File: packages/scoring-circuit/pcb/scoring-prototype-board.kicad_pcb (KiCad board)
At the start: 2 copper layers, 160 x 100 mm, 46 parts

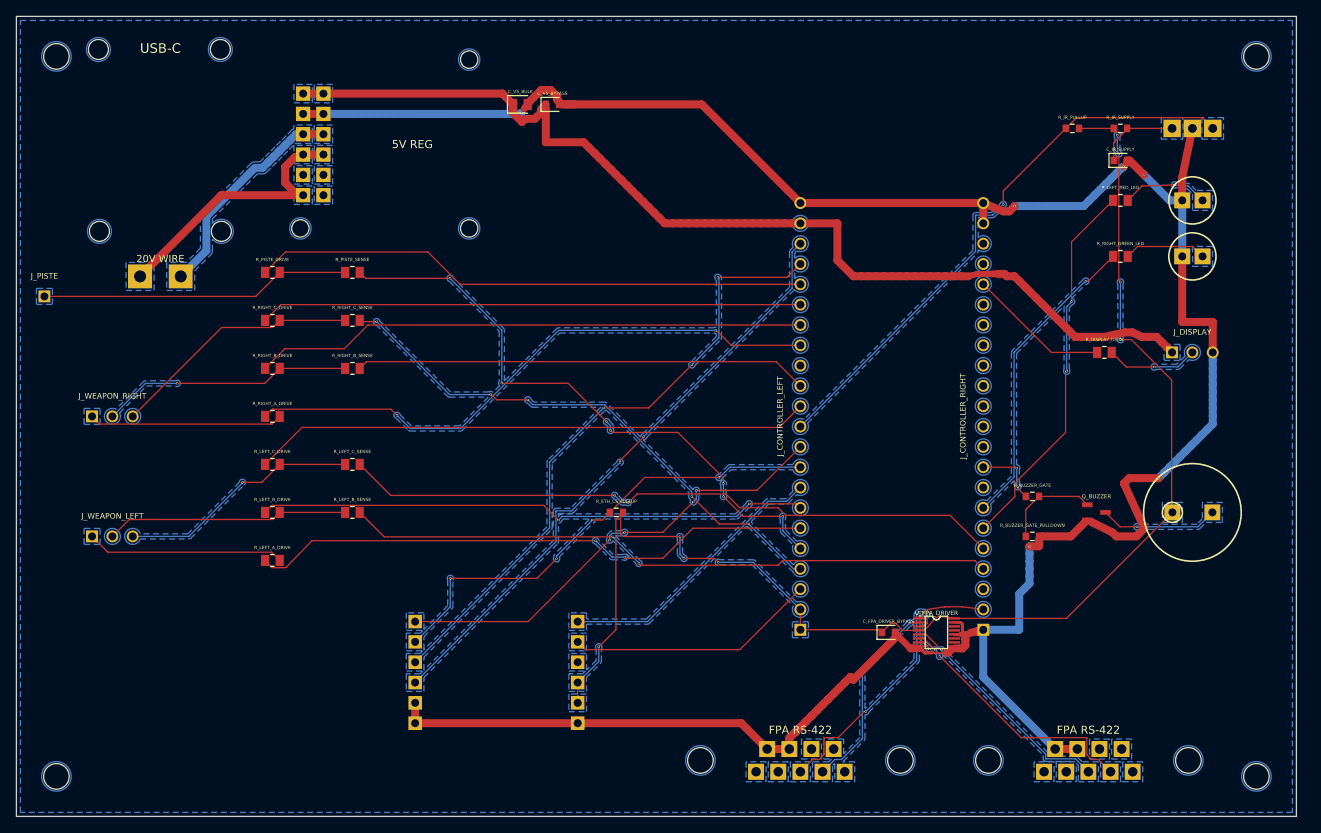
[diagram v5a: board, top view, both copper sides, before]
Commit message: feat(scoring-circuit): add FA-05 outputs and scoring lamps
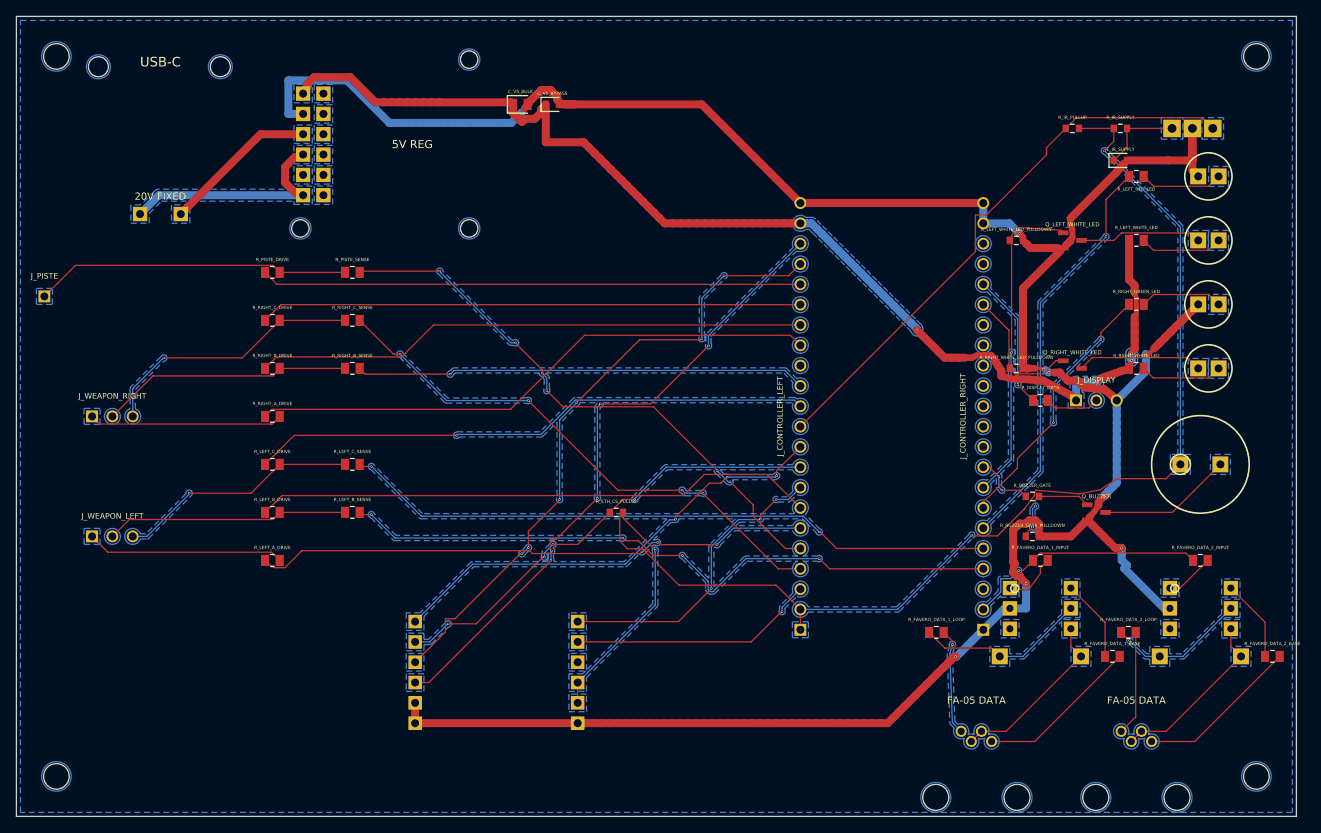
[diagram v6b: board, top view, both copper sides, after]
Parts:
- removed C_FPA_DRIVER_BYPASS: 100nF, tscircuit:C0603C104K3RACTU
- removed J_FPA_REPEATER_1, J_FPA_REPEATER_2: 182-009-113R161, tscircuit:182-009-113R161
- removed U_FPA_DRIVER: AM26LV31EIPWR, tscircuit:AM26LV31EIPWR
- removed the U_USB_C_PD at (37.9, 68.4)
- added D_FAVERO_DATA_1: 1N4004-E3/54, tscircuit:1N4004-E3_54, F.Cu at (148.0, 130.0)
- added D_FAVERO_DATA_2: 1N4004-E3/54, tscircuit:1N4004-E3_54, F.Cu at (168.0, 130.0)
- added J_FAVERO_DATA_1: 5520250-2, tscircuit:5520250-2, F.Cu at (140.0, 144.0)
- added J_FAVERO_DATA_2: 5520250-2, tscircuit:5520250-2, F.Cu at (160.0, 144.0)
- added LED_LEFT_WHITE: WP7113QWC/D, tscircuit:WP7113QWC_D, F.Cu at (169.0, 78.0)
- added LED_RIGHT_WHITE: WP7113QWC/D, tscircuit:WP7113QWC_D, F.Cu at (169.0, 94.0)
- added Q_LEFT_WHITE_LED: BSS138-7-F, tscircuit:BSS138-7-F, F.Cu at (152.0, 78.0)
- added Q_RIGHT_WHITE_LED: BSS138-7-F, tscircuit:BSS138-7-F, F.Cu at (152.0, 94.0)
- added R_FAVERO_DATA_1_BASE: 680kΩ, tscircuit:RC0805FR-07680KL, F.Cu at (157.0, 130.0)
- added R_FAVERO_DATA_1_INPUT: 330Ω, tscircuit:RC0805FR-07330RL, F.Cu at (148.0, 118.0)
- added R_FAVERO_DATA_1_LOOP: 82Ω, tscircuit:RC0805FR-0782RL, F.Cu at (135.0, 127.0)
- added R_FAVERO_DATA_2_BASE: 680kΩ, tscircuit:RC0805FR-07680KL, F.Cu at (177.0, 130.0)
- added R_FAVERO_DATA_2_INPUT: 330Ω, tscircuit:RC0805FR-07330RL, F.Cu at (168.0, 118.0)
- added R_FAVERO_DATA_2_LOOP: 82Ω, tscircuit:RC0805FR-0782RL, F.Cu at (159.0, 127.0)
- added R_LEFT_WHITE_LED: 330Ω, tscircuit:RC0805FR-07330RL, F.Cu at (160.0, 78.0)
- added R_LEFT_WHITE_LED_PULLDOWN: 100kΩ, tscircuit:RC0603FR-07100KL, F.Cu at (145.0, 78.0)
- added R_RIGHT_WHITE_LED: 330Ω, tscircuit:RC0805FR-07330RL, F.Cu at (160.0, 94.0)
- added R_RIGHT_WHITE_LED_PULLDOWN: 100kΩ, tscircuit:RC0603FR-07100KL, F.Cu at (145.0, 94.0)
- added U_FAVERO_DATA_1: 4N32M, tscircuit:4N32M, F.Cu at (148.0, 124.0)
- added U_FAVERO_DATA_2: 4N32M, tscircuit:4N32M, F.Cu at (168.0, 124.0)
- added U_USB_C_PD: 5807, tscircuit:5807, F.Cu at (37.9, 65.3)
- moved J_DISPLAY 13.4 mm to (155.0, 98.0)
- moved R_DISPLAY_DATA 10.0 mm to (148.0, 98.0)
- moved LED_RIGHT_GREEN 6.32 mm to (169.0, 86.0)
- moved R_RIGHT_GREEN_LED 6.32 mm to (160.0, 86.0)
- moved BZ_SCORING 6.08 mm to (168.0, 106.0)
- moved LED_LEFT_RED 3.61 mm to (169.0, 70.0)
- moved R_LEFT_RED_LED 3.61 mm to (160.0, 70.0)
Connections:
- J_CONTROLLER_RIGHT pad 17: (no net) -> LED_RIGHT_WHITE_DRIVE
- J_CONTROLLER_RIGHT pad 2: FPA_TX -> FAVERO_DATA_TX
- J_CONTROLLER_RIGHT pad 8: (no net) -> LED_LEFT_WHITE_DRIVE
- U_V5_REGULATOR pad 11: U_USB_C_PD.PD_20V to U_V5_REGULATOR.VIN_1 -> U_USB_C_PD.PD_VOUT to U_V5_REGULATOR.VIN_1
- U_V5_REGULATOR pad 2: V5 -> (no net)
- U_V5_REGULATOR pad 4: APP_GND -> (no net)
- U_V5_REGULATOR pad 6: U_USB_C_PD.APP_GND to U_V5_REGULATOR.GND_IN_1 -> (no net)
- U_V5_REGULATOR pad 7: U_USB_C_PD.PD_20V to U_V5_REGULATOR.VIN_1 -> U_USB_C_PD.PD_VOUT to U_V5_REGULATOR.VIN_1
- U_V5_REGULATOR pad 8: U_USB_C_PD.PD_20V to U_V5_REGULATOR.VIN_1 -> (no net)
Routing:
- net LED_LEFT_WHITE_DRIVE: track 0.00 -> 40.3 mm, vias 0 -> 1
- net U_USB_C_PD.PD_20V to U_V5_REGULATOR.VIN_1: track 35.3 -> 0.00 mm
- net U_FPA_DRIVER.DRIVER_2_POSITIVE to J_FPA_REPEATER_2.TX_POS: track 32.3 -> 0.00 mm, vias 2 -> 0
- net U_FPA_DRIVER.DRIVER_1_NEGATIVE to J_FPA_REPEATER_1.TX_NEG: track 31.3 -> 0.00 mm, vias 2 -> 0
- net FAVERO_DATA_TX: track 0.00 -> 30.5 mm, vias 0 -> 1
- net U_USB_C_PD.PD_VOUT to U_V5_REGULATOR.VIN_1: track 0.00 -> 29.5 mm
- net U_FPA_DRIVER.DRIVER_2_NEGATIVE to J_FPA_REPEATER_2.TX_NEG: track 28.7 -> 0.00 mm, vias 1 -> 0
- net U_FPA_DRIVER.DRIVER_1_POSITIVE to J_FPA_REPEATER_1.TX_POS: track 24.7 -> 0.00 mm, vias 1 -> 0
- net U_FAVERO_DATA_2.EMITTER to J_FAVERO_DATA_2.DATA_A: track 0.00 -> 22.1 mm
- net U_FAVERO_DATA_1.EMITTER to J_FAVERO_DATA_1.DATA_A: track 0.00 -> 22.1 mm
- net U_FAVERO_DATA_1.COLLECTOR to R_FAVERO_DATA_1_LOOP.pin1: track 0.00 -> 21.5 mm
- net R_FAVERO_DATA_2_BASE.pin2 to J_FAVERO_DATA_2.OUTER_B: track 0.00 -> 20.4 mm
- net R_FAVERO_DATA_1_BASE.pin2 to J_FAVERO_DATA_1.OUTER_B: track 0.00 -> 20.4 mm
- net U_FAVERO_DATA_2.COLLECTOR to R_FAVERO_DATA_2_LOOP.pin1: track 0.00 -> 17.5 mm, vias 0 -> 1
- net LED_RIGHT_WHITE_DRIVE: track 0.00 -> 17.0 mm
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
